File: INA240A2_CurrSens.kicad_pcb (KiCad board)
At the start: 2 copper layers, 31.4 x 28.2 mm, 17 parts, among them U1 INA240A2D, U2 INA240A2D

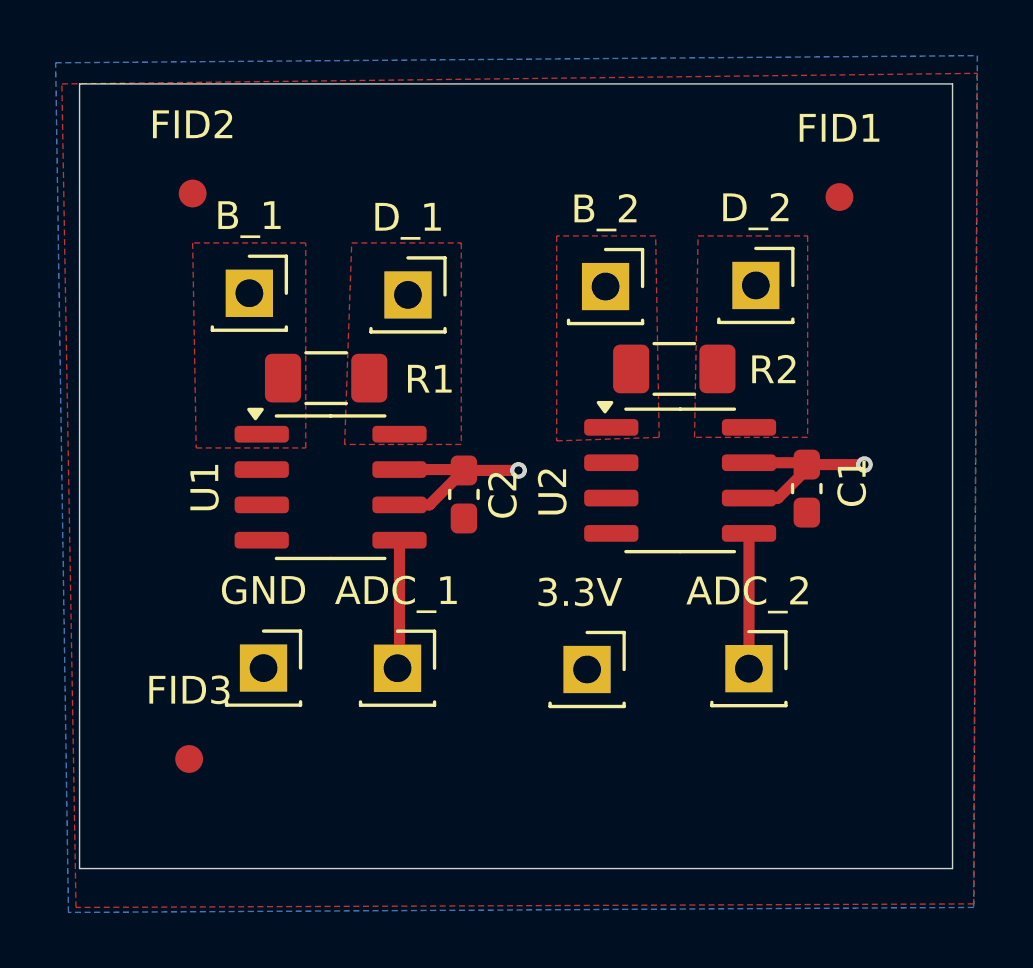
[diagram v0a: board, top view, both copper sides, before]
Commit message: adjusted filled zones to correct drc
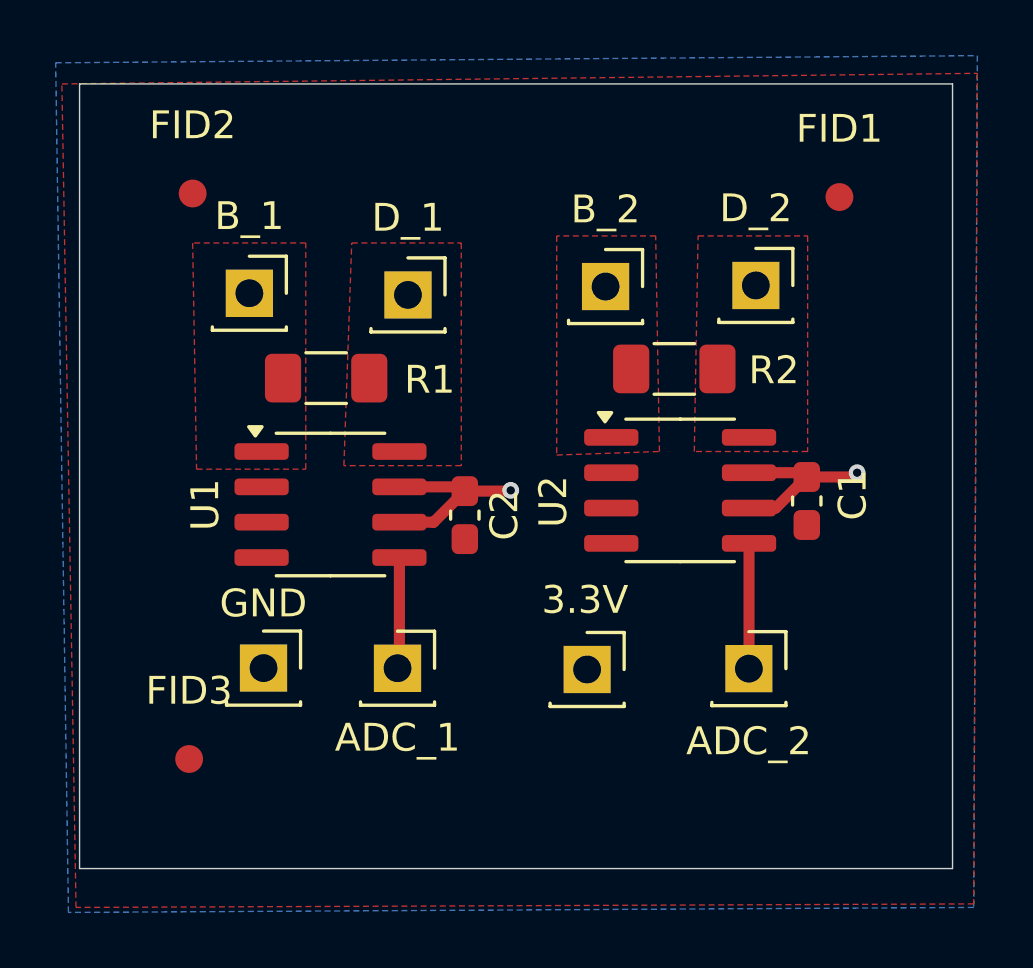
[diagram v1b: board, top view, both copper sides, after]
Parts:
- moved C2 0.74 mm to (120.1, 78.6)
- moved U1 0.62 mm to (115.3, 78.2)
- moved C1 0.45 mm to (132.4, 78.1)
- moved U2 0.36 mm to (127.9, 77.7)
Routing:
- net +3.3V: track 14.0 -> 13.4 mm
- net /ADC_1: track 4.63 -> 4.10 mm
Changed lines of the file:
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@@
 		(tags "Through hole socket strip THT 1x01 2.54mm single row")
 		(property "Reference" "ADC_1"
-			(at 0 -2.77 0)
+			(at 0 2.499 0)
 			(layer "F.SilkS")
 			(effects
@@
 		(tags "Through hole socket strip THT 1x01 2.54mm single row")
 		(property "Reference" "ADC_2"
-			(at 0 -2.77 0)
+			(at 0 2.611 0)
 			(layer "F.SilkS")
 			(effects
@@
 		(tags "Through hole socket strip THT 1x01 2.54mm single row")
 		(property "Reference" "GND"
-			(at 0 -2.77 0)
+			(at -0.007 -2.322 0)
 			(layer "F.SilkS")
 			(effects
@@
 	(footprint "Capacitor_SMD:C_0603_1608Metric_Pad1.08x0.95mm_HandSolder"
 		(layer "F.Cu")
-		(at 132.43 77.66 90)
+		(at 132.43 78.105 90)
 		(descr "Capacitor SMD 0603 (1608 Metric), square (rectangular) end terminal, IPC-7351 nominal with elongated pad for handsoldering. (Body size source: IPC-SM-782 page 76, https://www.pcb-3d.com/wordpress/wp-content/uploads/ipc-sm-782a_amendment_1_and_2.pdf), generated with kicad-footprint-generator")
 		(tags "capacitor handsolder")
@@
 	(footprint "Package_SO:SOIC-8_3.9x4.9mm_P1.27mm"
 		(layer "F.Cu")
-		(at 127.88 77.365)
+		(at 127.88 77.724)
 		(descr "SOIC, 8 Pin (JEDEC MS-012AA, https://www.analog.com/media/en/package-pcb-resources/package/pkg_pdf/soic_narrow-r/r_8.pdf), generated with kicad-footprint-generator ipc_gullwing_generator.py")
 		(tags "SOIC SO")
@@
 		(tags "Through hole socket strip THT 1x01 2.54mm single row")
 		(property "Reference" "3.3V"
-			(at -0.29 -2.75 0)
+			(at -0.076667 -2.499 0)
 			(layer "F.SilkS")
 			(effects
@@
 	(footprint "Package_SO:SOIC-8_3.9x4.9mm_P1.27mm"
 		(layer "F.Cu")
-		(at 115.32 77.61)
+		(at 115.316 78.232)
 		(descr "SOIC, 8 Pin (JEDEC MS-012AA, https://www.analog.com/media/en/package-pcb-resources/package/pkg_pdf/soic_narrow-r/r_8.pdf), generated with kicad-footprint-generator ipc_gullwing_generator.py")
 		(tags "SOIC SO")
@@
 	(footprint "Capacitor_SMD:C_0603_1608Metric_Pad1.08x0.95mm_HandSolder"
 		(layer "F.Cu")
-		(at 120.11 77.87 90)
+		(at 120.142 78.613 90)
 		(descr "Capacitor SMD 0603 (1608 Metric), square (rectangular) end terminal, IPC-7351 nominal with elongated pad for handsoldering. (Body size source: IPC-SM-782 page 76, https://www.pcb-3d.com/wordpress/wp-content/uploads/ipc-sm-782a_amendment_1_and_2.pdf), generated with kicad-footprint-generator")
 		(tags "capacitor handsolder")
@@
 	)
 	(segment
-		(start 122.0725 77.0075)
-		(end 122.09 76.99)
-		(width 0.2)
+		(start 131.3135 78.359)
+		(end 132.43 77.2425)
+		(width 0.4)
 		(layer "F.Cu")
 		(net 1)
 	)
 	(segment
-		(start 132.43 76.97)
-		(end 132.43 76.7975)
-		(width 0.2)
+		(start 130.355 77.089)
+		(end 132.2765 77.089)
+		(width 0.4)
 		(layer "F.Cu")
 		(net 1)
 	)
 	(segment
-		(start 120.11 77.0075)
-		(end 122.0725 77.0075)
+		(start 117.791 77.597)
+		(end 119.9885 77.597)
 		(width 0.4)
 		(layer "F.Cu")
@@
 	)
 	(segment
-		(start 117.795 76.975)
-		(end 120.0775 76.975)
+		(start 132.2765 77.089)
+		(end 132.43 77.2425)
 		(width 0.4)
 		(layer "F.Cu")
@@
 	)
 	(segment
-		(start 130.355 76.73)
-		(end 132.3625 76.73)
+		(start 117.791 78.867)
+		(end 119.0255 78.867)
 		(width 0.4)
 		(layer "F.Cu")
@@
 	)
 	(segment
-		(start 132.3625 76.73)
-		(end 132.43 76.7975)
-		(width 0.2)
+		(start 119.0255 78.867)
+		(end 120.142 77.7505)
+		(width 0.4)
 		(layer "F.Cu")
 		(net 1)
 	)
 	(segment
-		(start 130.355 78)
-		(end 131.4 78)
+		(start 121.7665 77.7505)
+		(end 121.793 77.724)
 		(width 0.4)
 		(layer "F.Cu")
@@
 	)
 	(segment
-		(start 118.8725 78.245)
-		(end 120.11 77.0075)
+		(start 132.43 77.2425)
+		(end 134.0855 77.2425)
 		(width 0.4)
 		(layer "F.Cu")
@@
 	)
 	(segment
-		(start 132.43 76.7975)
-		(end 134.5025 76.7975)
+		(start 130.355 78.359)
+		(end 131.3135 78.359)
 		(width 0.4)
 		(layer "F.Cu")
@@
 	)
 	(segment
-		(start 120.0775 76.975)
-		(end 120.11 77.0075)
-		(width 0.2)
+		(start 119.9885 77.597)
+		(end 120.142 77.7505)
+		(width 0.4)
 		(layer "F.Cu")
 		(net 1)
 	)
 	(segment
-		(start 117.795 78.245)
-		(end 118.8725 78.245)
+		(start 120.142 77.7505)
+		(end 121.7665 77.7505)
 		(width 0.4)
 		(layer "F.Cu")
@@
 	)
 	(segment
-		(start 131.4 78)
-		(end 132.43 76.97)
+		(start 134.0855 77.2425)
+		(end 134.239 77.089)
 		(width 0.4)
 		(layer "F.Cu")
@@
 	)
 	(via
-		(at 134.5025 76.7975)
+		(at 134.239 77.089)
 		(size 0.6)
 		(drill 0.3)
@@
 	)
 	(via
-		(at 122.0725 77.0075)
+		(at 121.793 77.724)
 		(size 0.6)
 		(drill 0.3)
@@
 	)
 	(segment
-		(start 117.795 79.515)
-		(end 117.795 84.045)
+		(start 117.791 84.049)
+		(end 117.725 84.115)
 		(width 0.4)
 		(layer "F.Cu")
@@
 	)
 	(segment
-		(start 130.355 79.27)
+		(start 117.791 80.137)
+		(end 117.791 84.049)
+		(width 0.4)
+		(layer "F.Cu")
+		(net 7)
+	)
+	(segment
+		(start 130.355 79.629)
 		(end 130.355 84.125)
 		(width 0.4)
@@
 		(start 130.355 84.125)
 		(end 130.35 84.13)
-		(width 0.2)
+		(width 0.4)
 		(layer "F.Cu")
 		(net 8)
@@
 		(polygon
 			(pts
-				(xy 123.444 68.58) (xy 123.444 75.946) (xy 127.127 75.819) (xy 127 68.58)
+				(xy 123.444 68.58) (xy 123.444 76.454) (xy 127.135907 76.326693) (xy 127 68.58)
 			)
 		)
@@
 		(polygon
 			(pts
-				(xy 128.397 75.819) (xy 128.524 68.58) (xy 132.461 68.58) (xy 132.461 75.819)
+				(xy 128.388088 76.327) (xy 128.524 68.58) (xy 132.461 68.58) (xy 132.461 76.327)
 			)
 		)
@@
 		(polygon
 			(pts
-				(xy 114.427 76.2) (xy 114.427 68.834) (xy 110.363 68.834) (xy 110.49 76.2)
+				(xy 114.427 76.962) (xy 114.427 68.834) (xy 110.363 68.834) (xy 110.503138 76.962)
 			)
 		)
@@
 		(polygon
 			(pts
-				(xy 116.078 68.834) (xy 120.015 68.834) (xy 120.015 76.073) (xy 115.824 76.073)
+				(xy 116.078 68.834) (xy 120.015 68.834) (xy 120.015 76.835) (xy 115.797263 76.835)
 			)
 		)

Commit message: adjusted board positioning to maintain signal integrity
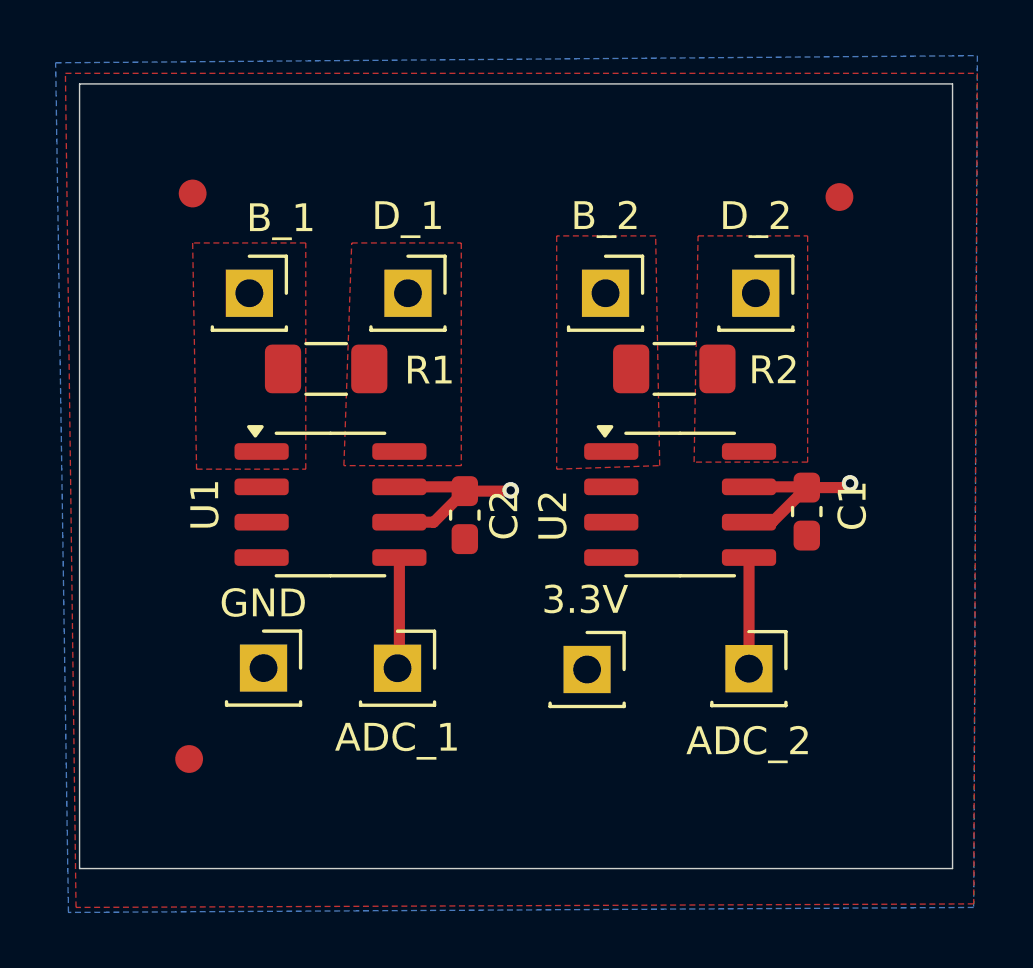
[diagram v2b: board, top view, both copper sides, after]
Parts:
- moved U2 0.51 mm to (127.9, 78.2)
- moved C1 0.38 mm to (132.4, 78.5)
- moved R1 0.33 mm to (115.2, 73.4)
- moved D_2 0.28 mm to (130.6, 70.6)
- moved B_2 0.24 mm to (125.2, 70.6)
- moved D_1 0.06 mm to (118.1, 70.6)
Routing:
- net /ADC_2: track 4.50 -> 4.00 mm
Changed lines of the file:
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@@
 			(at 0 -2.45 0)
 			(layer "F.SilkS")
+			(hide yes)
 			(effects
 				(font
@@
 			(at 0 -2.45 0)
 			(layer "F.SilkS")
+			(hide yes)
 			(effects
 				(font
@@
 	(footprint "Connector_PinSocket_2.54mm:PinSocket_1x01_P2.54mm_Vertical"
 		(layer "F.Cu")
-		(at 118.1 70.7)
+		(at 118.1 70.64)
 		(descr "Through hole straight socket strip, 1x01, 2.54mm pitch, single row (from Kicad 4.0.7), script generated")
 		(tags "Through hole socket strip THT 1x01 2.54mm single row")
@@
 		(tags "Through hole socket strip THT 1x01 2.54mm single row")
 		(property "Reference" "B_1"
-			(at 0 -2.77 0)
+			(at 1.138 -2.695 0)
 			(layer "F.SilkS")
 			(effects
@@
 	(footprint "Capacitor_SMD:C_0603_1608Metric_Pad1.08x0.95mm_HandSolder"
 		(layer "F.Cu")
-		(at 132.43 78.105 90)
+		(at 132.43 78.486 90)
 		(descr "Capacitor SMD 0603 (1608 Metric), square (rectangular) end terminal, IPC-7351 nominal with elongated pad for handsoldering. (Body size source: IPC-SM-782 page 76, https://www.pcb-3d.com/wordpress/wp-content/uploads/ipc-sm-782a_amendment_1_and_2.pdf), generated with kicad-footprint-generator")
 		(tags "capacitor handsolder")
@@
 	(footprint "Connector_PinSocket_2.54mm:PinSocket_1x01_P2.54mm_Vertical"
 		(layer "F.Cu")
-		(at 125.2 70.4)
+		(at 125.2 70.64)
 		(descr "Through hole straight socket strip, 1x01, 2.54mm pitch, single row (from Kicad 4.0.7), script generated")
 		(tags "Through hole socket strip THT 1x01 2.54mm single row")
@@
 	(footprint "Resistor_SMD:R_1206_3216Metric_Pad1.30x1.75mm_HandSolder"
 		(layer "F.Cu")
-		(at 115.16 73.69 180)
+		(at 115.16 73.36 180)
 		(descr "Resistor SMD 1206 (3216 Metric), square (rectangular) end terminal, IPC-7351 nominal with elongated pad for handsoldering. (Body size source: IPC-SM-782 page 72, https://www.pcb-3d.com/wordpress/wp-content/uploads/ipc-sm-782a_amendment_1_and_2.pdf), generated with kicad-footprint-generator")
 		(tags "resistor handsolder")
@@
 	(footprint "Package_SO:SOIC-8_3.9x4.9mm_P1.27mm"
 		(layer "F.Cu")
-		(at 127.88 77.724)
+		(at 127.88 78.232)
 		(descr "SOIC, 8 Pin (JEDEC MS-012AA, https://www.analog.com/media/en/package-pcb-resources/package/pkg_pdf/soic_narrow-r/r_8.pdf), generated with kicad-footprint-generator ipc_gullwing_generator.py")
 		(tags "SOIC SO")
@@
 			(at 0 -2.45 0)
 			(layer "F.SilkS")
+			(hide yes)
 			(effects
 				(font
@@
 		)
 		(property "Value" "Fiducial"
-			(at 0 2.45 0)
+			(at 0 4.38375 0)
 			(layer "F.Fab")
 			(effects
@@
 	(footprint "Connector_PinSocket_2.54mm:PinSocket_1x01_P2.54mm_Vertical"
 		(layer "F.Cu")
-		(at 130.6 70.36)
+		(at 130.6 70.64)
 		(descr "Through hole straight socket strip, 1x01, 2.54mm pitch, single row (from Kicad 4.0.7), script generated")
 		(tags "Through hole socket strip THT 1x01 2.54mm single row")
@@
 	)
 	(segment
-		(start 131.3135 78.359)
-		(end 132.43 77.2425)
-		(width 0.4)
-		(layer "F.Cu")
-		(net 1)
-	)
-	(segment
-		(start 130.355 77.089)
-		(end 132.2765 77.089)
+		(start 132.43 77.6235)
+		(end 133.8315 77.6235)
 		(width 0.4)
 		(layer "F.Cu")
@@
 	)
 	(segment
-		(start 132.2765 77.089)
-		(end 132.43 77.2425)
+		(start 132.4035 77.597)
+		(end 132.43 77.6235)
 		(width 0.4)
 		(layer "F.Cu")
@@
 	)
 	(segment
-		(start 132.43 77.2425)
-		(end 134.0855 77.2425)
+		(start 119.9885 77.597)
+		(end 120.142 77.7505)
 		(width 0.4)
 		(layer "F.Cu")
@@
 	)
 	(segment
-		(start 130.355 78.359)
-		(end 131.3135 78.359)
+		(start 130.355 78.867)
+		(end 131.1865 78.867)
 		(width 0.4)
 		(layer "F.Cu")
@@
 	)
 	(segment
-		(start 119.9885 77.597)
-		(end 120.142 77.7505)
+		(start 130.355 77.597)
+		(end 132.4035 77.597)
 		(width 0.4)
 		(layer "F.Cu")
@@
 	)
 	(segment
-		(start 120.142 77.7505)
-		(end 121.7665 77.7505)
+		(start 133.8315 77.6235)
+		(end 133.985 77.47)
 		(width 0.4)
 		(layer "F.Cu")
@@
 	)
 	(segment
-		(start 134.0855 77.2425)
-		(end 134.239 77.089)
+		(start 131.1865 78.867)
+		(end 132.43 77.6235)
+		(width 0.4)
+		(layer "F.Cu")
+		(net 1)
+	)
+	(segment
+		(start 120.142 77.7505)
+		(end 121.7665 77.7505)
 		(width 0.4)
 		(layer "F.Cu")
@@
 	)
 	(via
-		(at 134.239 77.089)
+		(at 133.985 77.47)
 		(size 0.6)
 		(drill 0.3)
@@
 	)
 	(segment
-		(start 130.355 79.629)
-		(end 130.355 84.125)
+		(start 130.355 84.125)
+		(end 130.35 84.13)
 		(width 0.4)
 		(layer "F.Cu")
@@
 	)
 	(segment
-		(start 130.355 84.125)
-		(end 130.35 84.13)
+		(start 130.355 80.137)
+		(end 130.355 84.125)
 		(width 0.4)
 		(layer "F.Cu")
@@
 		(polygon
 			(pts
-				(xy 123.444 68.58) (xy 123.444 76.454) (xy 127.135907 76.326693) (xy 127 68.58)
+				(xy 123.444 68.58) (xy 123.444 76.962) (xy 127.144814 76.834386) (xy 127 68.58)
 			)
 		)
@@
 		(polygon
 			(pts
-				(xy 128.388088 76.327) (xy 128.524 68.58) (xy 132.461 68.58) (xy 132.461 76.327)
+				(xy 128.381404 76.708) (xy 128.524 68.58) (xy 132.461 68.58) (xy 132.461 76.708)
 			)
 		)
@@
 		(polygon
 			(pts
-				(xy 105.664 63.119) (xy 138.557 62.738) (xy 138.43 92.583) (xy 106.172 92.71)
+				(xy 105.791 62.738) (xy 138.557 62.738) (xy 138.43 92.583) (xy 106.172 92.71)
 			)
 		)

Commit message: corrected layout pattern
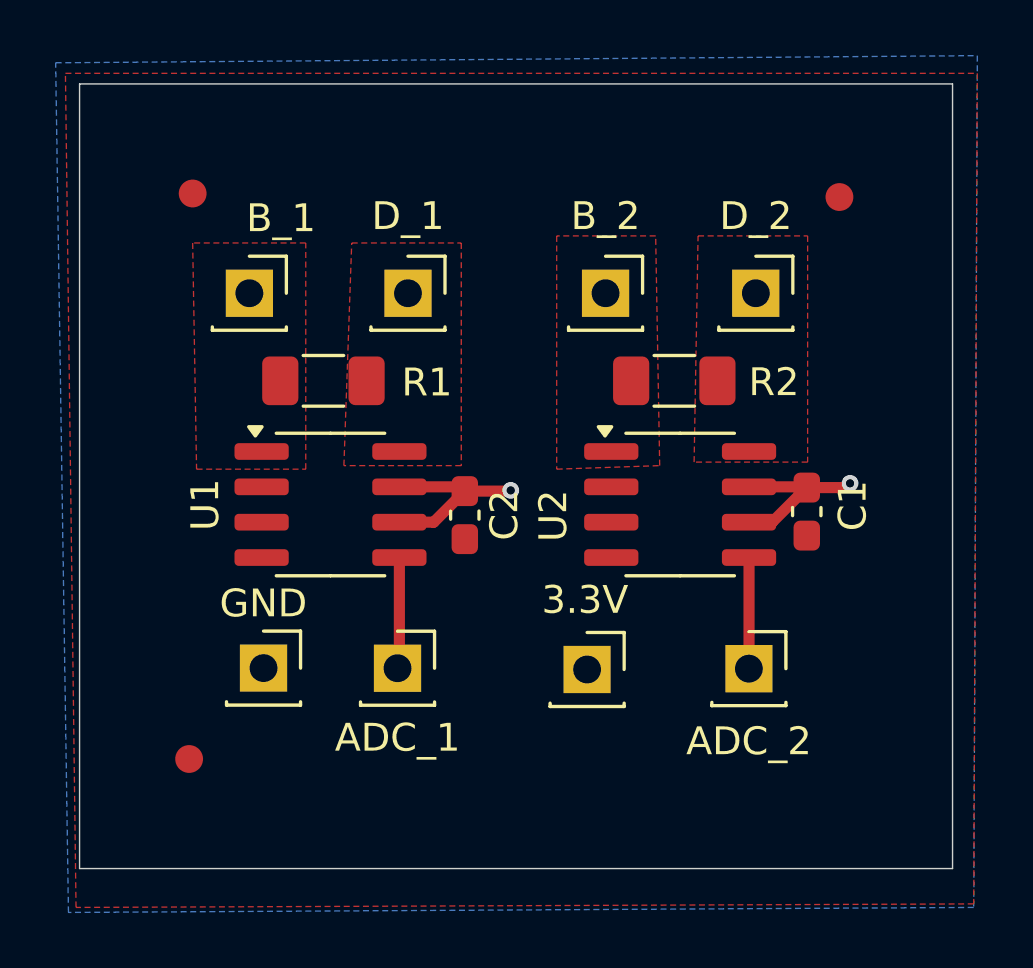
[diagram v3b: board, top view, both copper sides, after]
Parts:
- moved R1 0.44 mm to (115.1, 73.8)
- moved R2 0.43 mm to (127.7, 73.8)
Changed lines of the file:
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@@
 	(footprint "Resistor_SMD:R_1206_3216Metric_Pad1.30x1.75mm_HandSolder"
 		(layer "F.Cu")
-		(at 127.67 73.36 180)
+		(at 127.67 73.787 180)
 		(descr "Resistor SMD 1206 (3216 Metric), square (rectangular) end terminal, IPC-7351 nominal with elongated pad for handsoldering. (Body size source: IPC-SM-782 page 72, https://www.pcb-3d.com/wordpress/wp-content/uploads/ipc-sm-782a_amendment_1_and_2.pdf), generated with kicad-footprint-generator")
 		(tags "resistor handsolder")
@@
 	(footprint "Resistor_SMD:R_1206_3216Metric_Pad1.30x1.75mm_HandSolder"
 		(layer "F.Cu")
-		(at 115.16 73.36 180)
+		(at 115.062 73.787 180)
 		(descr "Resistor SMD 1206 (3216 Metric), square (rectangular) end terminal, IPC-7351 nominal with elongated pad for handsoldering. (Body size source: IPC-SM-782 page 72, https://www.pcb-3d.com/wordpress/wp-content/uploads/ipc-sm-782a_amendment_1_and_2.pdf), generated with kicad-footprint-generator")
 		(tags "resistor handsolder")
